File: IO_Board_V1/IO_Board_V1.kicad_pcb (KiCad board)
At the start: 2 copper layers, 79 x 49.5 mm, 92 parts, among them J1 USB_C_Receptacle_USB2.0, J10 IFM1, J11 FOURCHE, J12 BTN, J13 FOURCHE, J14 BTN, J15 CON_UART, J16 BTN, J17 FOURCHE, J18 IFM2, J19 IFM3, J2 CON_debug, J20 FOURCHE, J21 CON_I2C, J22 IFM4, J23 SPI, J24 BTN, J3 Conn_ARM_JTAG_SWD_10, J4 CON_CAN, J5 CON_CAN, J6 12V, J7 BTN, J8 BTN, J9 IFM0, SW1 BOOT, SW2 RST, U1 STM32F302C6Tx, U2 NCP1117-3.3_SOT223, U3 SN65HVD232, Y1 8MHz

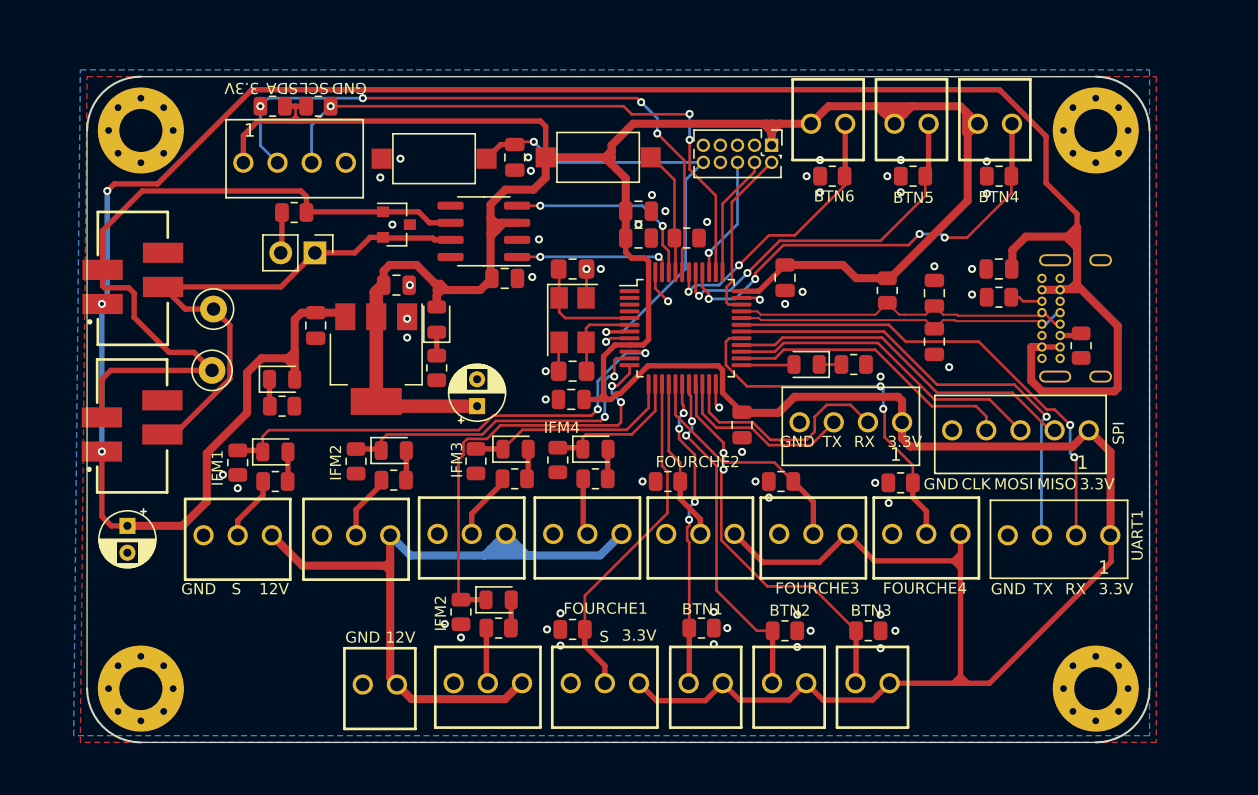
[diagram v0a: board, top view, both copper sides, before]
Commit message: IO prete, Pompe finir sérigraphie, Alim+AX12 à faire
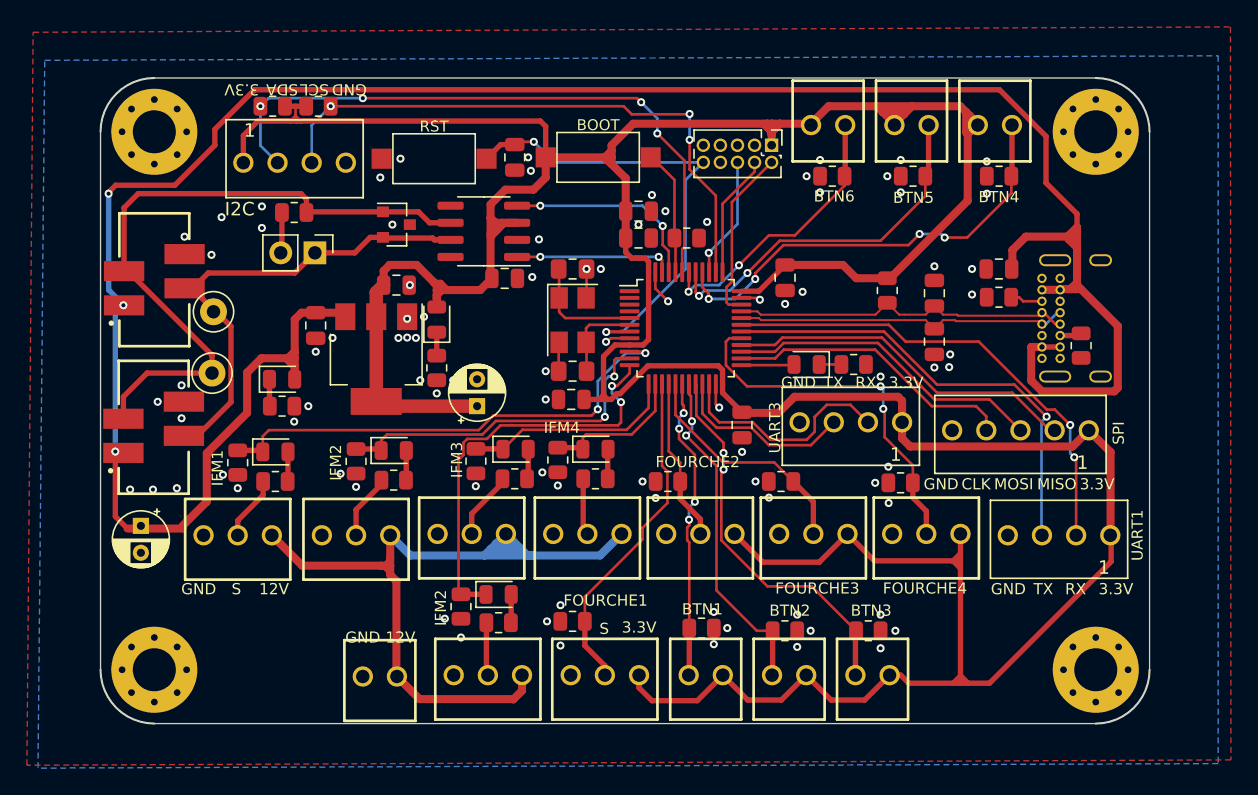
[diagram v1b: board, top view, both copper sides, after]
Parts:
- moved H4 1.72 mm to (90.5, 144.6)
- moved J5 1.60 mm to (90.5, 126.6)
- moved J4 1.60 mm to (90.5, 115.6)
- moved H3 1.40 mm to (160.5, 144.6)
- moved H2 1.00 mm to (90.5, 104.6)
- moved C3 1.00 mm to (89.5, 133.9)
- moved J11 0.60 mm to (124.0, 145.3)
- moved J12 0.60 mm to (137.7, 145.3)
- moved J14 0.60 mm to (143.9, 145.3)
- moved J18 0.60 mm to (115.3, 145.3)
- moved J6 0.60 mm to (107.3, 145.4)
- moved J7 0.60 mm to (131.5, 145.3)
- moved R13 0.60 mm to (121.6, 141.0)
- moved D7 0.40 mm to (116.1, 139.0)
- moved R20 0.40 mm to (116.1, 141.1)
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- renumbered SW1 to BOOT, SW2 to RST
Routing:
- net /CANL: track 56.0 -> 50.4 mm
- net /CANH: track 39.8 -> 35.4 mm
- net +3V3: track 319.0 -> 321.3 mm
- net /IO6: track 29.3 -> 28.7 mm
- net /IO4: track 23.3 -> 22.7 mm
- net /IO0: track 25.6 -> 25.0 mm
- net /IO5: track 25.9 -> 25.3 mm
- net +12V: track 60.2 -> 60.8 mm
- net +5V: track 177.7 -> 178.2 mm
- net GND: vias 59 -> 89
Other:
- board size 79 x 49.5 mm -> 78 x 48 mm
- board text added: "I2C"
- board text added: "UART3"
